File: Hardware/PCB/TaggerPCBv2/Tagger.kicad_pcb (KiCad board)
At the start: 2 copper layers, 35.6 x 105.3 mm, 24 parts, among them J1 Aim_Laser, J2 Shoot_B, J3 Aim_B, J4 Speaker, J5 Shoot_laser, J6 Neopixel, J7 IR_RCV, J8 Display, J9 Power, Q1 BC547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

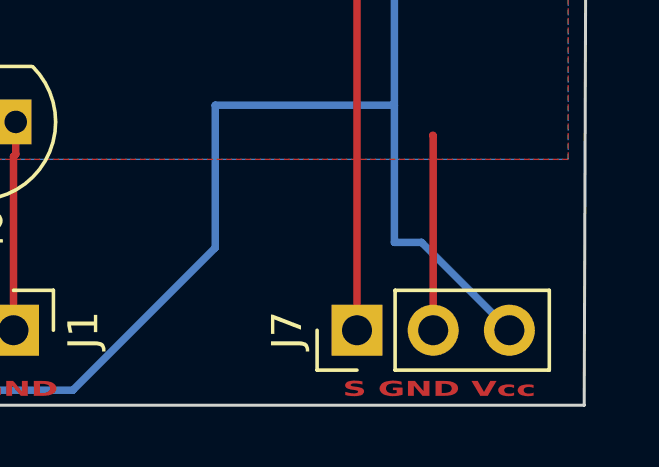
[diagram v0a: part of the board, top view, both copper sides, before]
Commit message: Made a plan for a easier Audio Amplifier circuit.
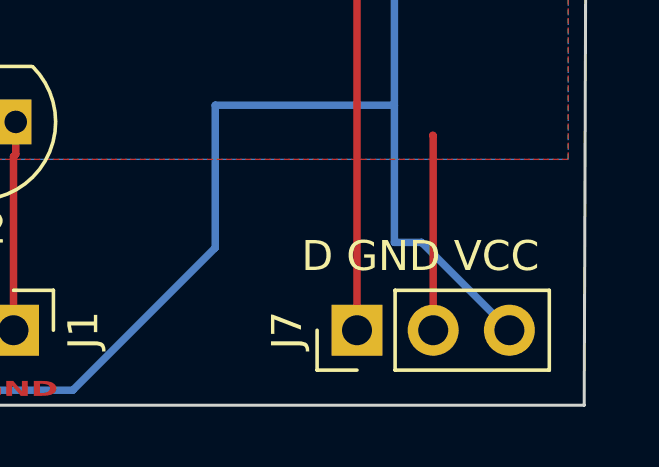
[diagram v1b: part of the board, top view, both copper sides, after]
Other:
- board text added: "D GND VCC"
- board text removed: "S GND Vcc"
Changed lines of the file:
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@@
         (effects (font (size 1 1) (thickness 0.15)))
     )
-    (fp_text value "IR_RCV" (at 3.75 2.275 180) (layer "F.Fab")
+    (fp_text value "IR_RCV" (at 4.425 2.275 180) (layer "F.Fab")
         (effects (font (size 1 1) (thickness 0.15)))
     )
@@
     (effects (font (size 0.5 0.8) (thickness 0.125) bold) (justify left bottom))
   )
-  (gr_text "S GND Vcc" (at 144.25 162.25) (layer "F.Cu")
-    (effects (font (size 0.5 0.8) (thickness 0.1) bold) (justify left bottom))
-  )
   (gr_text "Vcc GND" (at 129.5 162.25) (layer "F.Cu")
     (effects (font (size 0.5 0.8) (thickness 0.125) bold) (justify left bottom))
   )
+  (gr_text "D GND VCC" (at 142.875 158.115) (layer "F.SilkS")
+    (effects (font (size 1 1) (thickness 0.15)) (justify left bottom))
+  )
   (segment (start 138.43 130.0914) (end 138.43 126.344) (width 0.25) (layer "F.Cu") (net 1))
